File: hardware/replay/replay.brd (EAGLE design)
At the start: 34.9 x 31.8 mm, 19 parts, among them J1 SQUALL_HEADER, J2 5.5x2.1mm Barrel, U1 LT3083, U2 LT3083, U3 MAX5483

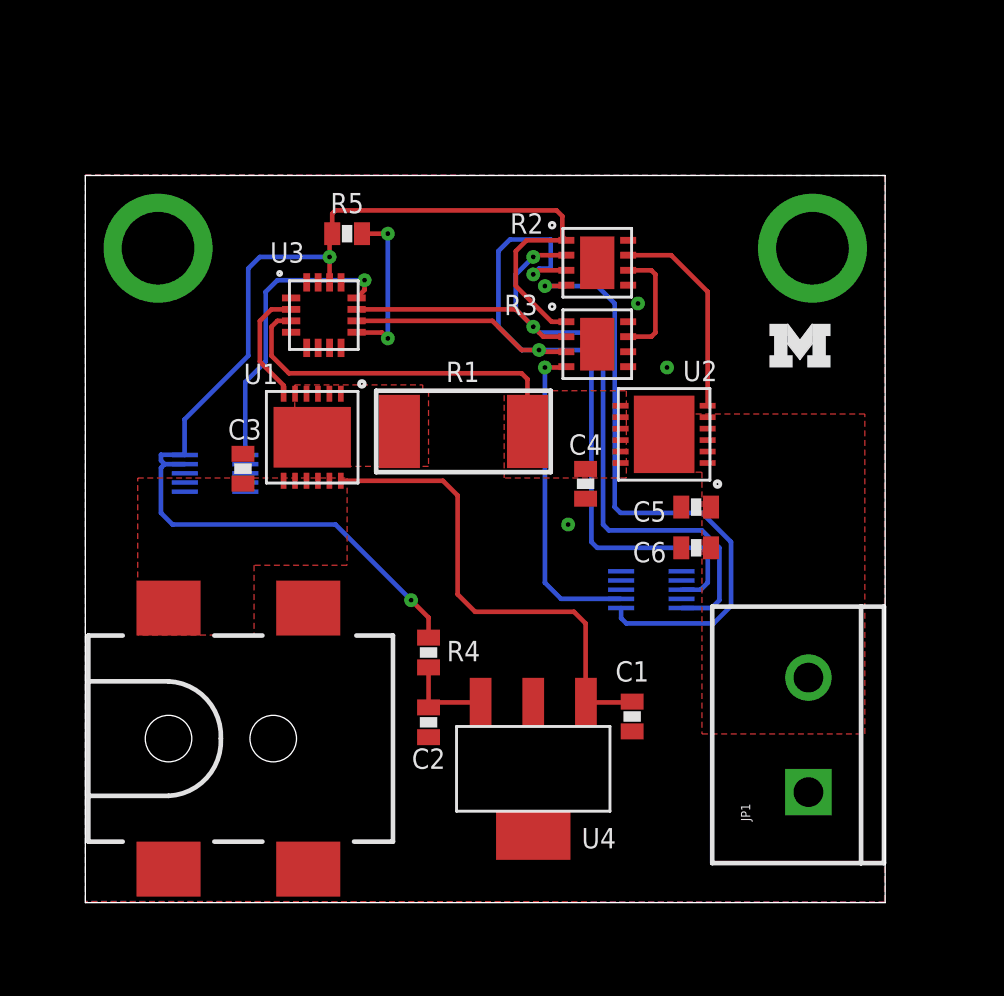
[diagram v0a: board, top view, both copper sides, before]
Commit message: board layed out with switches
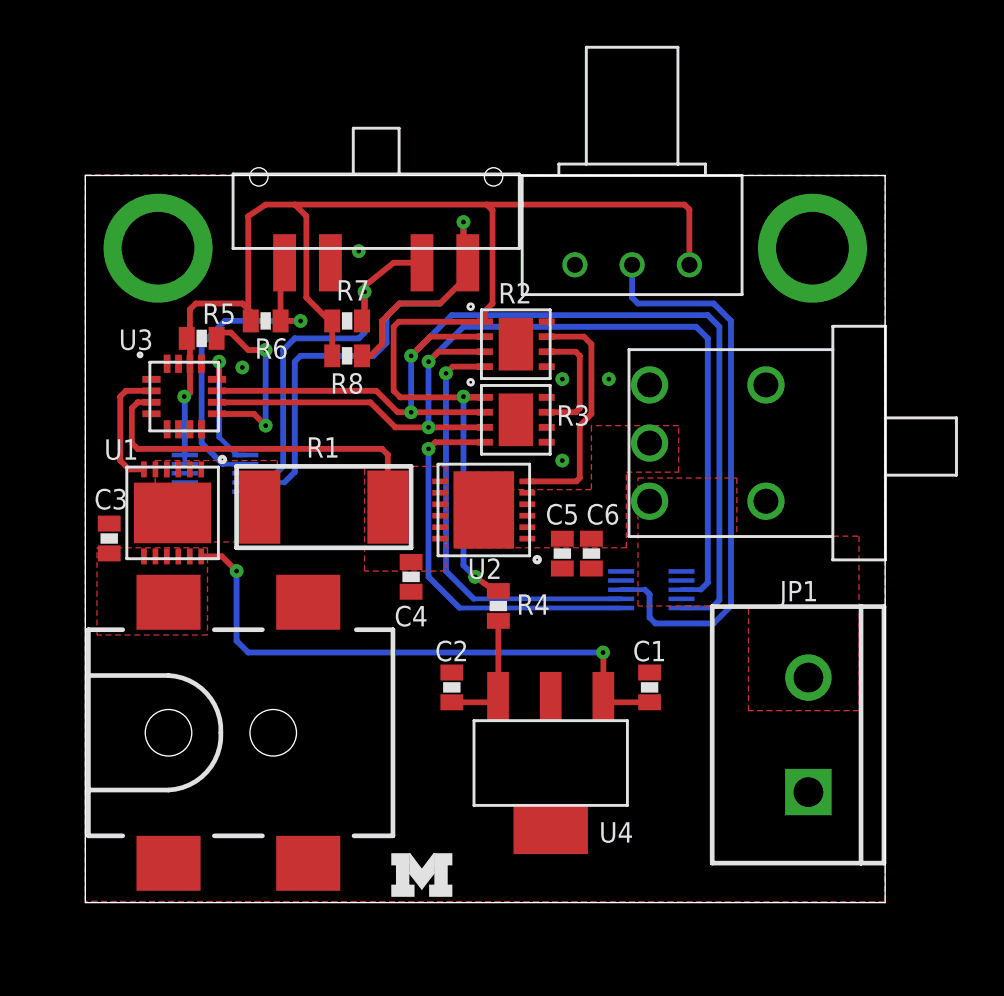
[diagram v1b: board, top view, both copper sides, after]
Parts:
- added R6, R7, R8: 10k, passives:0603-RES
- added R9: 0-10k, pots:3310C
- added SW1: CSS-1310TB, switches:JSM07011
- added SW2: 500ASSP, switches:500ASSP
- U3: value MAX5483 -> (none)
- moved LOGO1 28.4 mm to (13.4, 0.25)
- moved C4 8.64 mm to (14.2, 14.2)
- moved U2 8.54 mm to (17.4, 17.1)
- moved R5 7.82 mm to (5.08, 24.6)
- moved U3 7.06 mm to (4.32, 22.1)
- moved R1 6.93 mm to (10.4, 17.3)
- moved U1 6.93 mm to (3.81, 17.0)
- moved C3 6.59 mm to (1.04, 15.9)
- moved C5 6.19 mm to (20.8, 15.2), turned to 270 degrees
- moved R2 5.03 mm to (18.8, 24.4)
- moved R3 4.85 mm to (18.8, 21.1)
- moved C6 4.58 mm to (22.1, 15.2), turned to 270 degrees
- moved R4 3.66 mm to (18.0, 13.0)
- moved C2 1.83 mm to (16.0, 9.40), turned to 90 degrees
- moved C1 1.48 mm to (24.6, 9.40), turned to 90 degrees
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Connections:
- new net OUTS: JP1.2, SW2.1
- new net POT_OUT: J1.B5, R9.2
- new net S1: J1.A4, R6.1, SW1.4
- new net S2: J1.A6, R7.1, SW1.2
- new net S3: J1.A8, R8.1, SW1.1
- net 3V3: now also R6.2, R7.2, R8.2, R9.1
- net GND: now also R9.3, SW1.3
- net OUT: now also SW2.2; no longer JP1.2
- net V_SET_CS1: now also J1.B7; no longer J1.B9
- net V_SET_CS2: now also J1.B9; no longer J1.B7
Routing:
- net S3: track 0.00 -> 28.3 mm, vias 0 -> 1
- net POT_OUT: track 0.00 -> 24.9 mm
- net 3V3: track 53.3 -> 71.1 mm, vias 2 -> 3
- net S2: track 0.00 -> 16.9 mm, vias 0 -> 1
- net S1: track 0.00 -> 14.9 mm, vias 0 -> 1
- net SCLK: track 35.6 -> 46.3 mm
- net V_SET_CS1: track 27.4 -> 18.6 mm
- net I_SET_CS: track 12.9 -> 5.58 mm
- net VIN: track 21.3 -> 25.3 mm, vias 0 -> 2
- net V_SET_CS2: track 14.0 -> 17.1 mm
- net MOSI: track 39.7 -> 42.6 mm
- net N$7: track 4.11 -> 5.59 mm
- net N$5: track 9.11 -> 10.5 mm
- net N$9: track 7.17 -> 8.52 mm
- added copper zone on layer 1, net OUTS

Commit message: updated parts on the board and started making a case
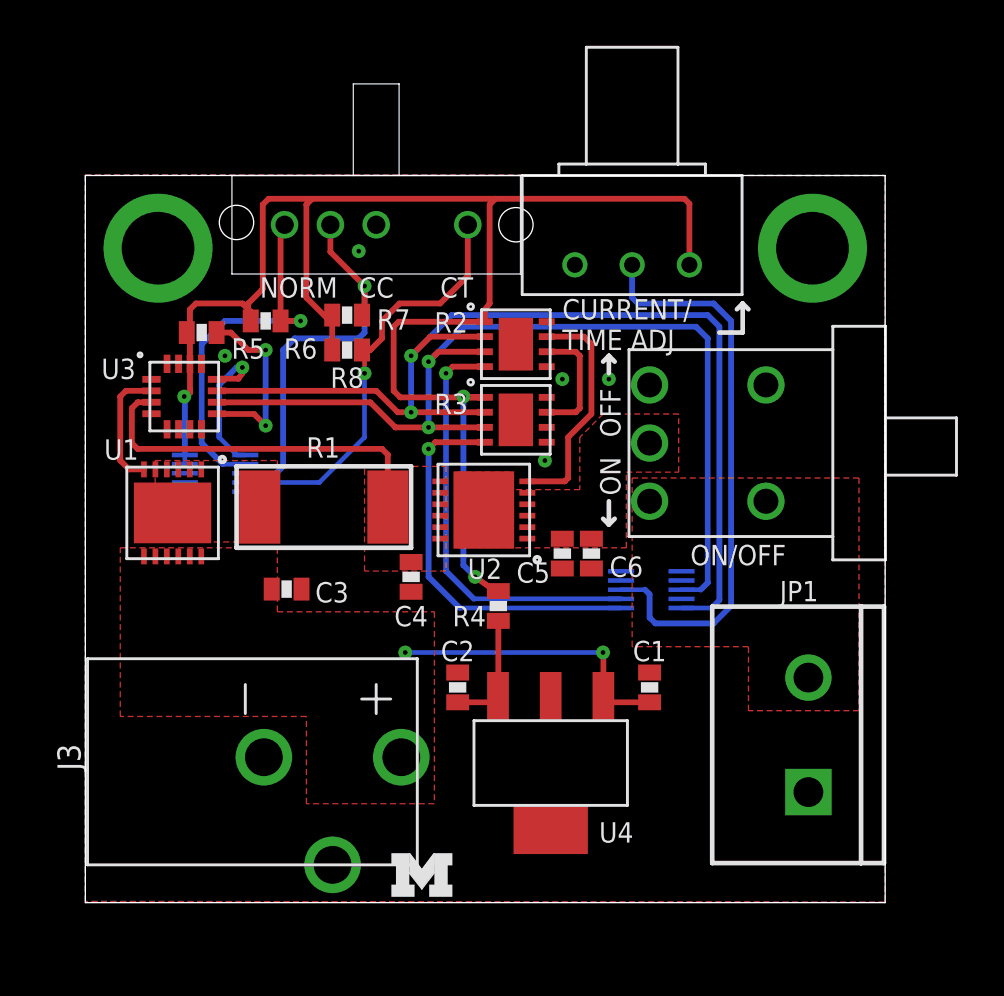
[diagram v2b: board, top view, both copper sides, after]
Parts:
- removed J2: 5.5x2.1mm Barrel, SparkFun-Connectors:POWER_JACK_SMD
- added J3: PJ-102AH, connector:PJ-102AH
- SW1: value CSS-1310TB -> OS103011; device switches:JSM07011 -> switches:OS103011
- moved C3 8.06 mm to (8.79, 13.7), turned to 0 degrees
- moved SW1 1.66 mm to (12.7, 29.6)
- moved C2 0.25 mm to (16.3, 9.40)
- moved R7 0.25 mm to (11.4, 25.7)
- moved R5 0.25 mm to (5.08, 24.9)
- moved R8 0.25 mm to (11.4, 24.1)
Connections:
- net GND: now also J3.2, J3.3, SW1.2; no longer J2.GND, J2.P$4, SW1.3
- net S2: now also SW1.3; no longer SW1.2
- net VIN: now also J3.1; no longer J2.VIN0
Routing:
- net VIN: track 25.3 -> 12.8 mm
- net S3: track 28.3 -> 18.5 mm
- net S1: track 14.9 -> 16.5 mm
- net I_SET_CS: track 5.58 -> 6.57 mm
- net S2: track 16.9 -> 17.6 mm
- net 3V3: track 71.1 -> 71.7 mm
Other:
- board text added: "CC"
- board text added: "CT"
- board text added: "CURRENT/ TIME ADJ"
- board text added: "NORM"
- board text added: "OFF"
- board text added: "ON"
- board text added: "ON/OFF"

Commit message: cleaned up schematic and changed screw terminal
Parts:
- removed JP1: (no value), SparkFun-Connectors:SCREWTERMINAL-5MM-2
- added J2: SCREW_TERMINAL, connector:PHEONIX-1935161
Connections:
- net GND: now also J2.1; no longer JP1.1
- net OUTS: now also J2.2; no longer JP1.2
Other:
- board text added: "+"
- board text added: "-"
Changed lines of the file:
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@@
 <setting verticaltext="up"/>
 </settings>
-<grid distance="0.01" unitdist="inch" unit="inch" style="lines" multiple="1" display="yes" altdistance="0.0025" altunitdist="inch" altunit="inch"/>
+<grid distance="0.001" unitdist="inch" unit="inch" style="lines" multiple="1" display="yes" altdistance="0.0025" altunitdist="inch" altunit="inch"/>
 <layers>
 <layer number="1" name="Top" color="4" fill="1" visible="yes" active="yes"/>
@@
 <text x="11.938" y="26.416" size="0.889" layer="25" font="vector">CC</text>
 <text x="15.494" y="26.416" size="0.889" layer="25" font="vector">CT</text>
+<text x="31.4198" y="1.9812" size="2.54" layer="25" font="vector" rot="R180">-</text>
+<text x="29.083" y="11.2014" size="2.54" layer="25" font="vector">+</text>
 </plain>
 <attributes>
@@
 <attribute name="NAME" x="23.622" y="14.224" size="0.889" layer="25" font="vector" ratio="12" align="bottom-center"/>
 </element>
-<element name="JP1" library="SparkFun-Connectors" package="SCREWTERMINAL-5MM-2" value="" x="31.5722" y="4.826" smashed="yes" rot="R90">
-<attribute name="NAME" x="32.004" y="14.0462" size="0.889" layer="25" font="vector" rot="R180"/>
-<attribute name="VALUE" x="30.3022" y="3.556" size="0.4064" layer="27" rot="R90"/>
-</element>
 <element name="SW2" library="switches" package="500ASSP" value="500ASSP" x="24.638" y="20.066" smashed="yes" rot="R270">
 <attribute name="DIGIKEY" value="EG2483-ND" x="24.638" y="20.066" size="1.778" layer="27" rot="R270" display="off"/>
@@
 <element name="SW1" library="switches" package="OS103011" value="OS103011" x="12.7" y="29.6" smashed="yes" rot="R180">
 <attribute name="DIGIKEY" value="CKN9561-ND" x="12.7" y="29.6" size="1.778" layer="27" rot="R180" display="off"/>
+</element>
+<element name="J2" library="connector" package="PHEONIX-1935161" value="SCREW_TERMINAL" x="29.8958" y="3.8354" smashed="yes" rot="R90">
+<attribute name="DIGIKEY" value="277-1667-ND" x="29.8958" y="3.8354" size="1.778" layer="27" rot="R90" display="off"/>
+<attribute name="NAME" x="34.6202" y="12.5984" size="0.889" layer="25" font="vector" rot="R180"/>
 </element>
 </elements>
@@
 <contactref element="C2" pad="2"/>
 <contactref element="C4" pad="2"/>
-<contactref element="C3" pad="2"/>
 <contactref element="C5" pad="2"/>
 <contactref element="C6" pad="2"/>
-<contactref element="JP1" pad="1"/>
 <contactref element="R9" pad="3"/>
 <via x="6.096" y="23.876" extent="1-16" drill="0.2032"/>
@@
 <contactref element="J3" pad="3"/>
 <contactref element="SW1" pad="2"/>
+<contactref element="J2" pad="1"/>
+<contactref element="C3" pad="2"/>
 </signal>
 <signal name="OUT1">
@@
 <contactref element="U2" pad="8"/>
 <contactref element="U2" pad="7"/>
-<contactref element="U3" pad="3"/>
 <contactref element="C4" pad="1"/>
 <polygon width="0.2032" layer="1" thermals="no">
@@
 <vertex x="12.192" y="14.478"/>
 </polygon>
-<wire x1="2.888" y1="21.848" x2="2.29" y2="21.848" width="0.254" layer="1"/>
 <wire x1="2.29" y1="21.848" x2="2.032" y2="21.59" width="0.254" layer="1"/>
 <wire x1="2.032" y1="21.59" x2="2.032" y2="20.066" width="0.254" layer="1"/>
@@
 <wire x1="13.208" y1="19.558" x2="13.208" y2="17.278" width="0.254" layer="1"/>
 <wire x1="13.208" y1="17.278" x2="13.214" y2="17.272" width="0.254" layer="1"/>
+<contactref element="U3" pad="3"/>
+<wire x1="2.29" y1="21.848" x2="2.888" y2="21.848" width="0.2032" layer="1"/>
 </signal>
 <signal name="N$3">
@@
 <contactref element="U4" pad="1"/>
 <contactref element="C1" pad="1"/>
-<contactref element="C3" pad="1"/>
 <polygon width="0.2032" layer="1" thermals="no" rank="2">
 <vertex x="1.524" y="8.128"/>
@@
 <wire x1="22.606" y1="10.922" x2="13.97" y2="10.922" width="0.2032" layer="16"/>
 <via x="13.97" y="10.922" extent="1-16" drill="0.2032"/>
+<contactref element="C3" pad="1"/>
 </signal>
 <signal name="N$5">
@@
 <contactref element="R2" pad="1"/>
 <contactref element="R3" pad="1"/>
-<contactref element="J1" pad="A3"/>
-<contactref element="J1" pad="A1"/>
 <contactref element="R5" pad="2"/>
 <contactref element="R9" pad="1"/>
@@
 <via x="4.318" y="22.098" extent="1-16" drill="0.2032"/>
 <wire x1="4.318" y1="22.098" x2="4.3442" y2="22.0718" width="0.254" layer="16"/>
-<wire x1="4.3442" y1="22.0718" x2="4.3442" y2="19.5452" width="0.254" layer="16"/>
 <wire x1="17.446" y1="22.062" x2="16.8" y2="22.062" width="0.254" layer="1"/>
 <wire x1="16.8" y1="22.062" x2="16.51" y2="22.098" width="0.254" layer="1"/>
@@
 <wire x1="17.018" y1="14.224" x2="17.892" y2="13.604" width="0.254" layer="1"/>
 <wire x1="17.892" y1="13.604" x2="18.034" y2="13.604" width="0.254" layer="1"/>
-<wire x1="4.3442" y1="19.5452" x2="4.3442" y2="19.1452" width="0.2032" layer="16"/>
 <wire x1="10.78" y1="25.654" x2="10.668" y2="25.4" width="0.254" layer="1"/>
 <wire x1="10.668" y1="25.4" x2="9.652" y2="26.416" width="0.254" layer="1"/>
 <wire x1="9.652" y1="26.416" x2="9.652" y2="30.48" width="0.254" layer="1"/>
 <wire x1="9.652" y1="30.48" x2="9.906" y2="30.734" width="0.254" layer="1"/>
+<contactref element="J1" pad="A3"/>
+<contactref element="J1" pad="A1"/>
+<wire x1="4.3442" y1="19.5452" x2="4.3442" y2="19.1452" width="0.2032" layer="16"/>
+<wire x1="4.3442" y1="22.0718" x2="4.3442" y2="19.1452" width="0.2032" layer="16"/>
 </signal>
 <signal name="I_SET_CS">
@@
 </signal>
 <signal name="OUTS">
-<contactref element="JP1" pad="2"/>
 <contactref element="SW2" pad="1"/>
 <polygon width="0.254" layer="1" thermals="no" rank="2">
@@
 <vertex x="23.876" y="18.542"/>
 <vertex x="33.782" y="18.542"/>
-<vertex x="33.782" y="8.382"/>
-<vertex x="28.956" y="8.382"/>
-<vertex x="28.956" y="11.176"/>
+<vertex x="33.782" y="7.366"/>
+<vertex x="26.416" y="7.366"/>
+<vertex x="26.416" y="11.176"/>
 </polygon>
+<contactref element="J2" pad="2"/>
 </signal>
 <signal name="POT_OUT">

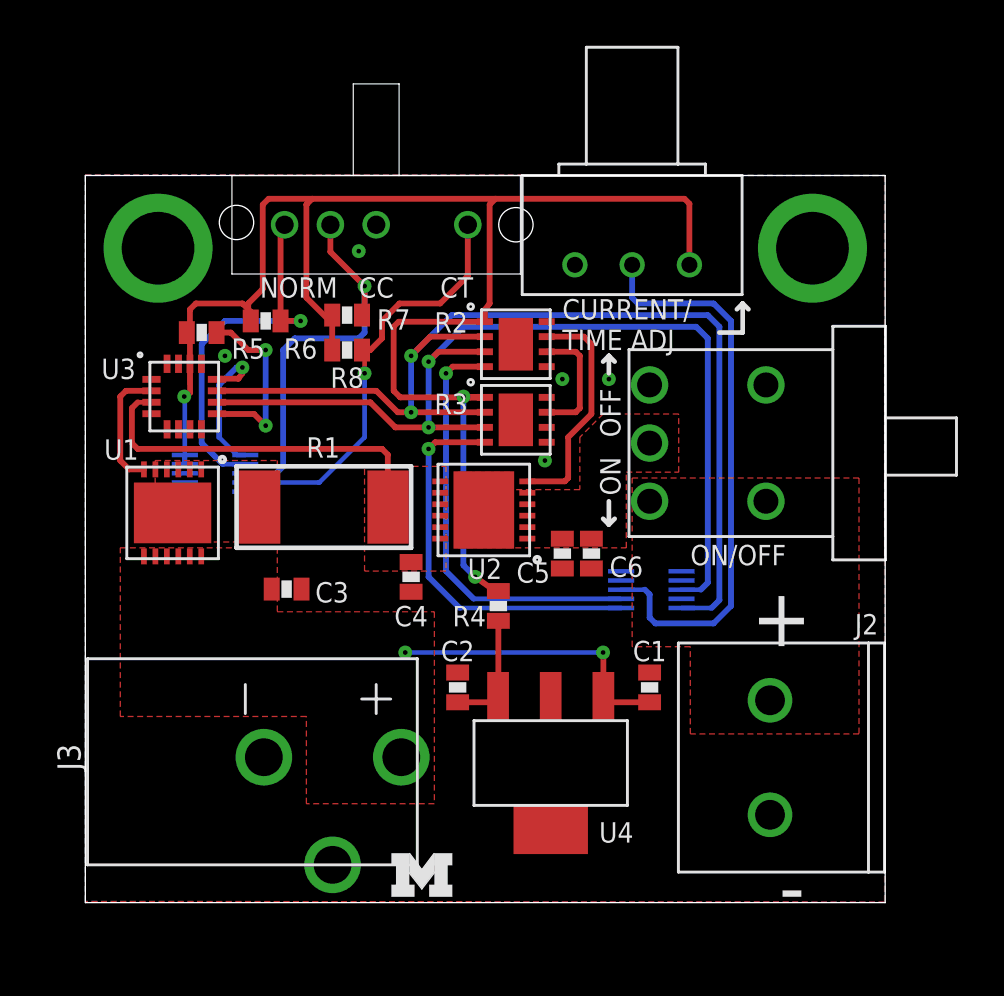
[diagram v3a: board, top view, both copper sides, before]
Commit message: added the shipped version of replay
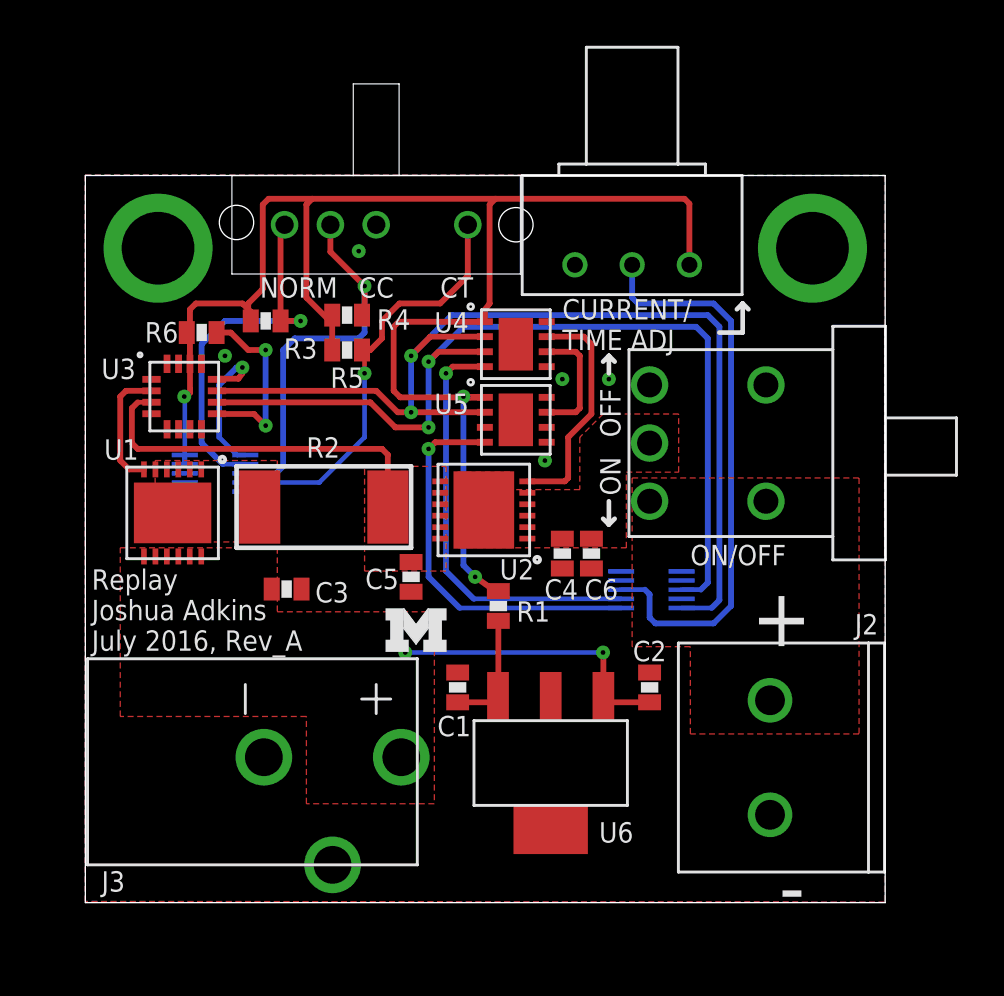
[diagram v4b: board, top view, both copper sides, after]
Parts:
- removed R8: 10k, passives:0603-RES
- removed R9: 0-10k, pots:3310C
- added U5: 0-200K, chips:TDFN-8/3MM
- added U6: (no value), chips:SOT-223
- C1: value 0.33uF -> 0.1uF
- C2: value 0.1uF -> 0.33uF
- C4: value 15uF -> 10uF
- C5: value 10uF -> 15uF
- R1: value .16 -> 0; device SparkFun-Passives:R2512 -> passives:0603-RES
- R2: value (none) -> .16; device chips:TDFN-8/3MM -> SparkFun-Passives:R2512
- R3: value (none) -> 10k; device chips:TDFN-8/3MM -> passives:0603-RES
- R4: value 0 -> 10k
- R5: value 10K -> 10k
- R6: value 10k -> 10K
- R7: value 10k -> 0-10k; device passives:0603-RES -> pots:3310C
- U3: value (none) -> 0-10K
- U4: value (none) -> 0-200K; device chips:SOT-223 -> chips:TDFN-8/3MM
- moved U4 18.4 mm to (18.8, 24.4), turned to 270 degrees
- moved R4 14.3 mm to (11.4, 25.7), turned to 180 degrees
- moved R7 13.9 mm to (23.9, 31.8)
- moved R3 11.7 mm to (7.87, 25.4), turned to 180 degrees
- moved R2 11.0 mm to (10.4, 17.3), turned to 0 degrees
- moved LOGO1 10.7 mm to (13.1, 10.9)
- moved R1 8.76 mm to (18.0, 13.0), turned to 90 degrees
- moved C1 8.38 mm to (16.3, 9.40)
- moved C2 8.38 mm to (24.6, 9.40)
- moved C4 6.68 mm to (20.8, 15.2)
- moved C5 6.68 mm to (14.2, 14.2)
- moved R5 6.40 mm to (11.4, 24.1)
- moved R6 2.84 mm to (5.08, 24.9)
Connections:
- new net U5: U5.3
- net 3V3: now also R1.2, R3.2, R7.1, U4.1, U5.1; no longer R2.1, R3.1, R7.2, R8.2, R9.1
- net GND: now also R7.3, U4.5, U5.5, U5.6, U6.2, U6.4; no longer R2.5, R3.5, R3.6, R9.3, U4.2, U4.4
- net MOSI: now also U4.3; no longer R2.3, R3.3
- net N$5: now also U4.7; no longer R2.7
- net N$6: now also U4.6, U5.7; no longer R2.6, R3.7
- net N$7: now also C1.1, R1.1, U6.3; no longer C2.1, R4.1, U4.3
- net N$9: now also R6.1; no longer R5.1
- net OUT: now also C4.1; no longer C5.1
- net OUT1: now also R2.1; no longer R1.1
- net POT_OUT: now also R7.2; no longer R9.2
- net S1: now also R3.1; no longer R6.1
- net S2: now also R4.1; no longer R7.1
- net S3: now also R5.1; no longer R8.1
- net SCLK: now also U4.2, U5.2; no longer R2.2, R3.2
- net VIN: now also C2.1, U6.1; no longer C1.1, U4.1
- net VIN2: now also C5.1, R2.2; no longer C4.1, R1.2
- net V_SET_CS1: now also U4.4; no longer R2.4
- net V_SET_CS2: now also U5.4; no longer R3.4
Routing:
- net MOSI: track 42.6 -> 40.2 mm
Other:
- board text added: "Replay Joshua Adkins July 2016, Rev_A"
